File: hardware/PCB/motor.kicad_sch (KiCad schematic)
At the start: 56 parts, among them J3 Cutting Tool, U4 BSC050N04LSG

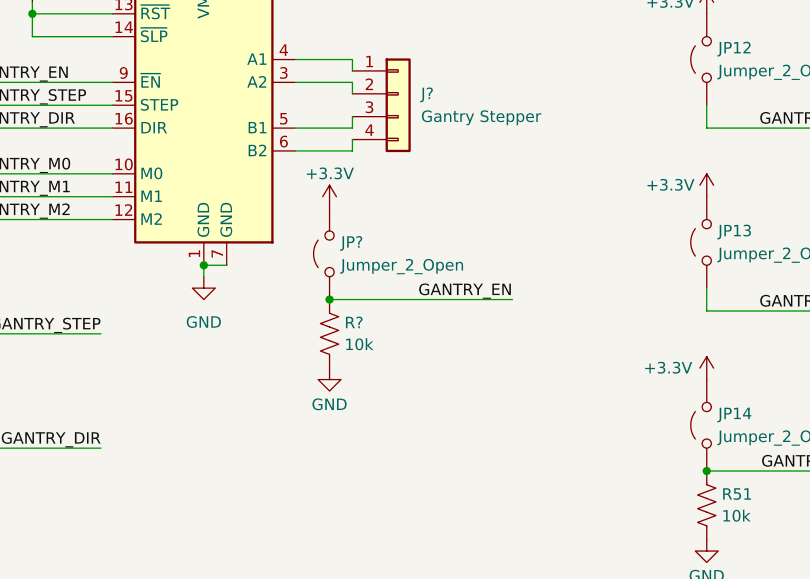
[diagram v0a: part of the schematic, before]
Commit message: Schematic - Motor Control Error
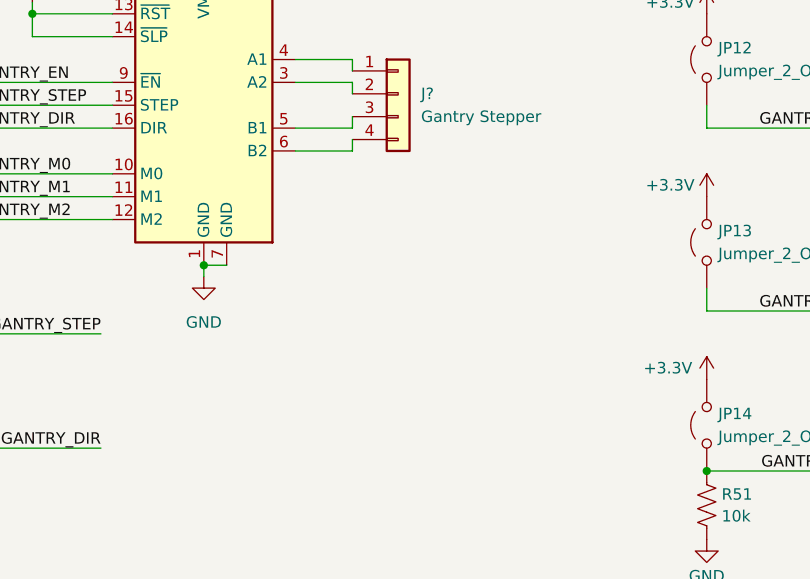
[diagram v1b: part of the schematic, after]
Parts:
- removed JP?: Jumper_2_Open, Connector_PinHeader_2.54mm:PinHeader_1x02_P2.54mm_Vertical, symbol Jumper:Jumper_2_Open
- removed R?: 10k, Resistor_SMD:R_0805_2012Metric, symbol Device:R_US
- added TP? (x2): TestPoint, symbol Connector:TestPoint
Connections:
- net EXTRUDER_DIR: now also TP?.1; no longer TP?.1
- net EXTRUDER_STEP: now also TP?.1; no longer TP?.1

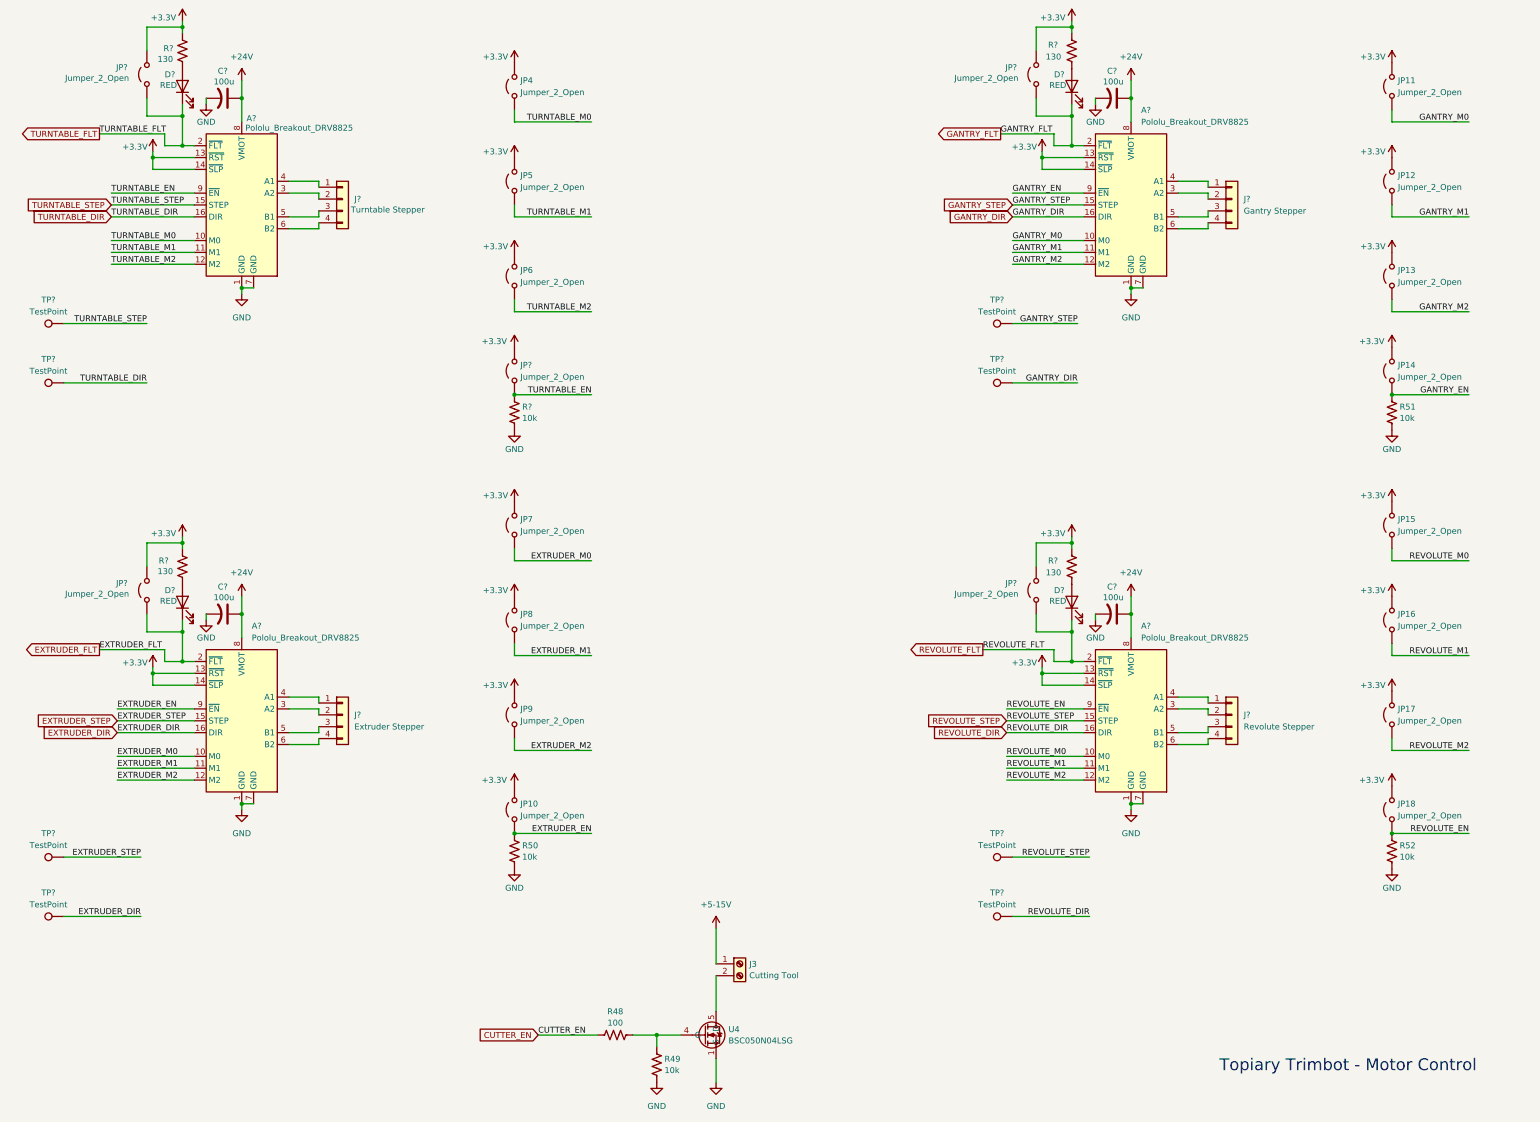
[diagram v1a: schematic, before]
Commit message: Synchronized schematic draft and reannotated all
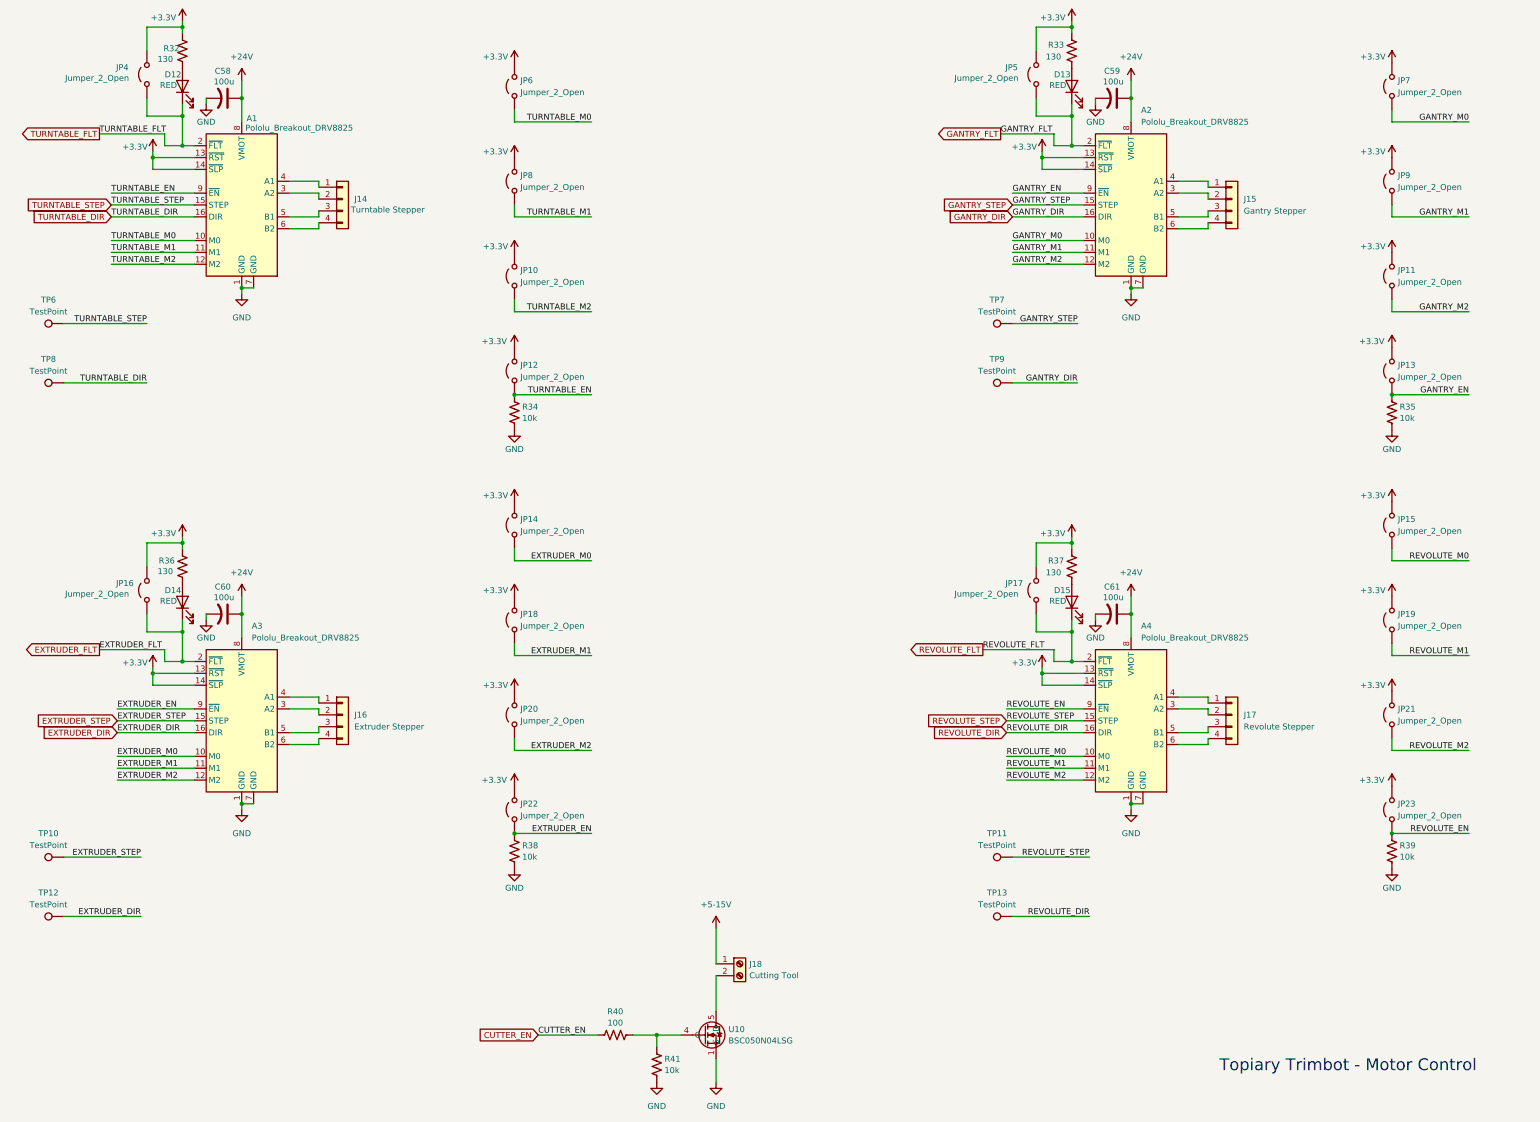
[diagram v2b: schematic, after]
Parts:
- J14, J15, J16, J17: renamed from J?; MANUFACTURER (none) -> Molex
- TP10, TP11, TP12, TP13, TP6, TP7, TP8, TP9: renamed from TP?; footprint (none) -> TestPoint:TestPoint_Pad_D1.5mm
- gave numbers to parts that had none: 22
- renumbered J3 to J18, JP6 to JP10, JP13 to JP11, JP14 to JP13, JP7 to JP14, JP8 to JP18, JP16 to JP19, JP9 to JP20, JP17 to JP21, JP10 to JP22, JP18 to JP23, JP4 to JP6, JP11 to JP7, JP5 to JP8, JP12 to JP9, R51 to R35, R50 to R38, R52 to R39, R48 to R40, R49 to R41, U4 to U10

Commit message: Finish first pass placement of parts on PCB, several updates and fixes to schematic included
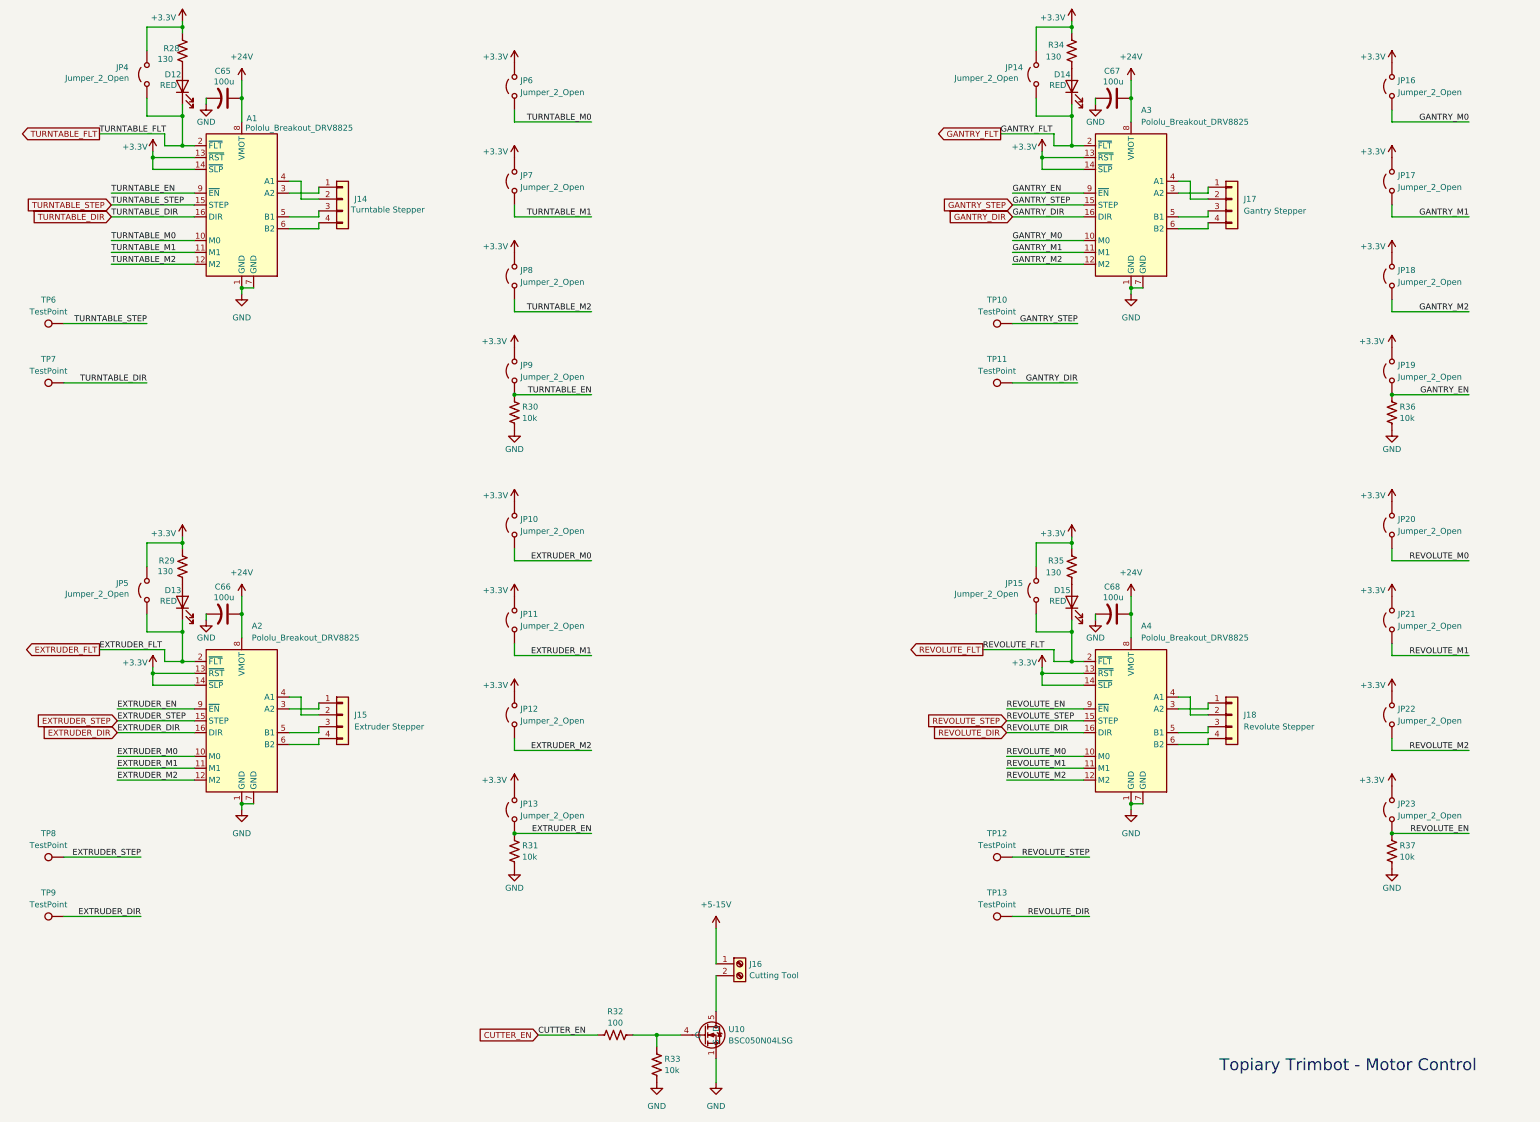
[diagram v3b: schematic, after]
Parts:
- renumbered A3 to A2, A2 to A3, C58 to C65, C60 to C66, C59 to C67, C61 to C68, D14 to D13, D13 to D14, J16 to J15, J18 to J16, J15 to J17, J17 to J18, JP14 to JP10, JP18 to JP11, JP20 to JP12, JP22 to JP13, JP5 to JP14, JP17 to JP15, JP7 to JP16, JP9 to JP17, JP11 to JP18, JP13 to JP19, JP15 to JP20, JP19 to JP21, JP21 to JP22, JP16 to JP5, JP8 to JP7, JP10 to JP8, JP12 to JP9, R32 to R28, R36 to R29, R34 to R30, R38 to R31, R40 to R32, R41 to R33, R33 to R34, R37 to R35, R35 to R36, R39 to R37, TP7 to TP10, TP9 to TP11, TP11 to TP12, TP8 to TP7, TP10 to TP8, TP12 to TP9
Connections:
- net at A4.3 (A2): now also J18.1 (Pin_1); no longer J18.2 (Pin_2)
- net at A4.4 (A1): now also J18.2 (Pin_2); no longer J18.1 (Pin_1)
- net at A2.3 (A2): now also J15.1 (Pin_1); no longer J15.2 (Pin_2)
- net at A2.4 (A1): now also J15.2 (Pin_2); no longer J15.1 (Pin_1)
- net at A3.3 (A2): now also J17.1 (Pin_1); no longer J17.2 (Pin_2)
- net at A3.4 (A1): now also J17.2 (Pin_2); no longer J17.1 (Pin_1)
- net at A1.3 (A2): now also J14.1 (Pin_1); no longer J14.2 (Pin_2)
- net at A1.4 (A1): now also J14.2 (Pin_2); no longer J14.1 (Pin_1)

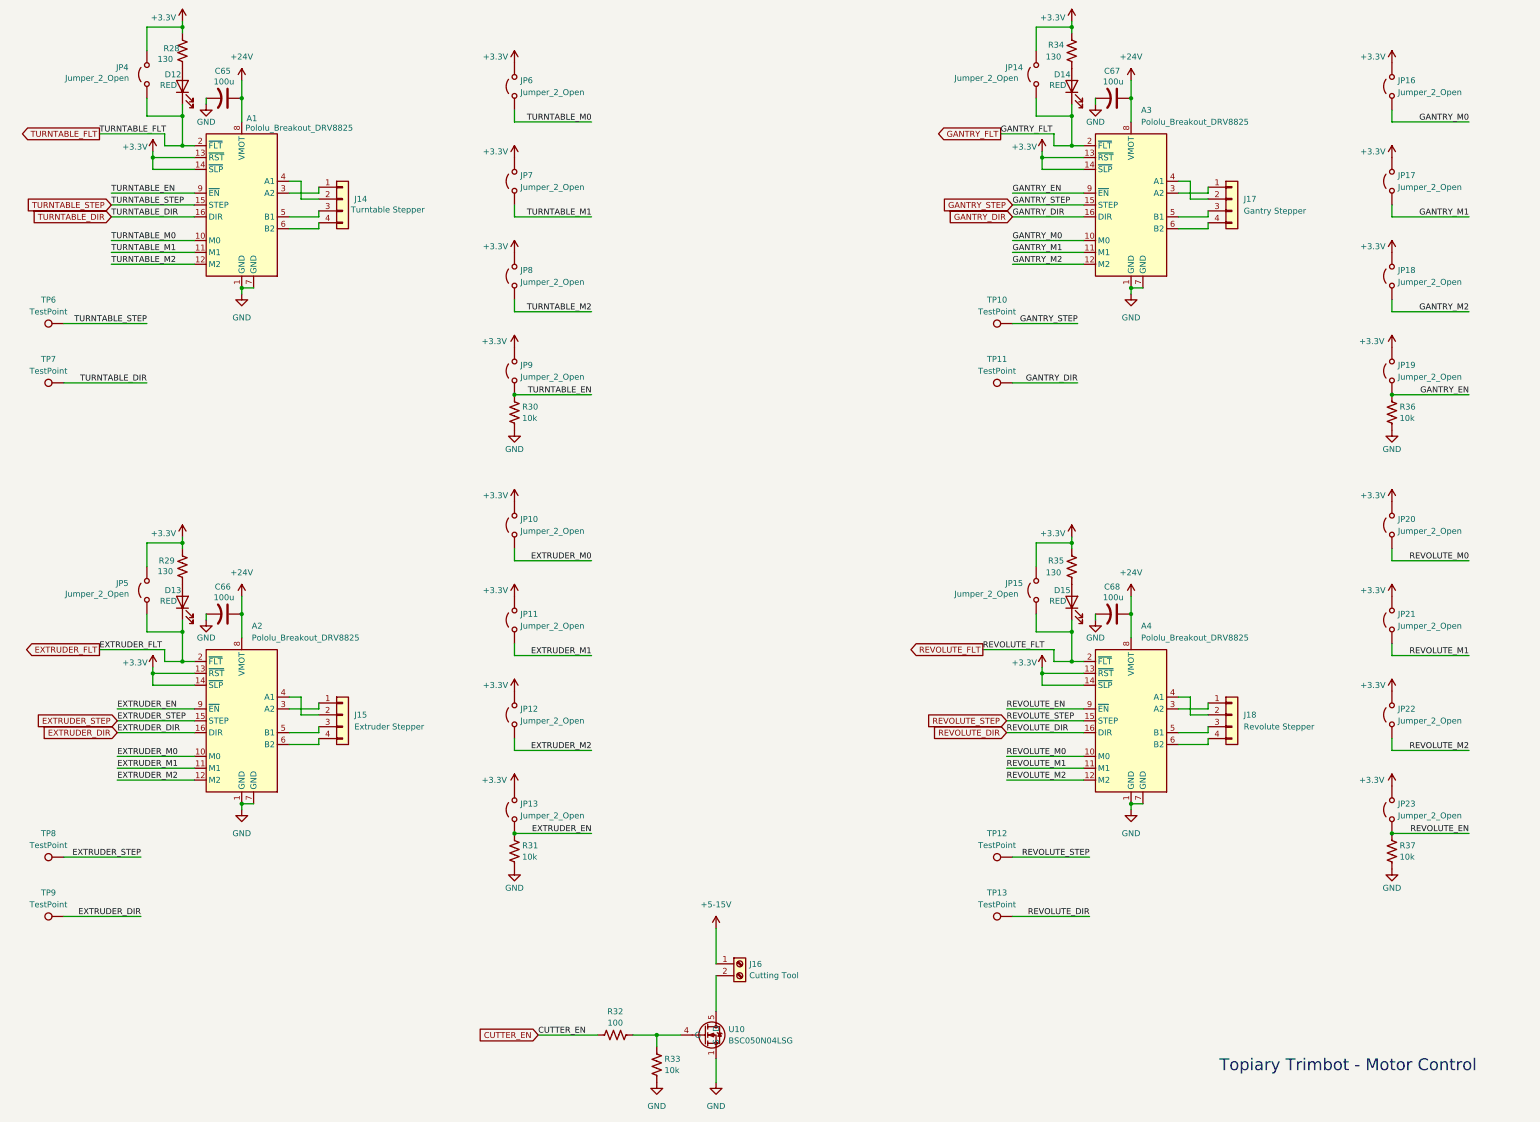
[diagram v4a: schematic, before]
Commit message: Continue layout, including swapping to linear BL driver
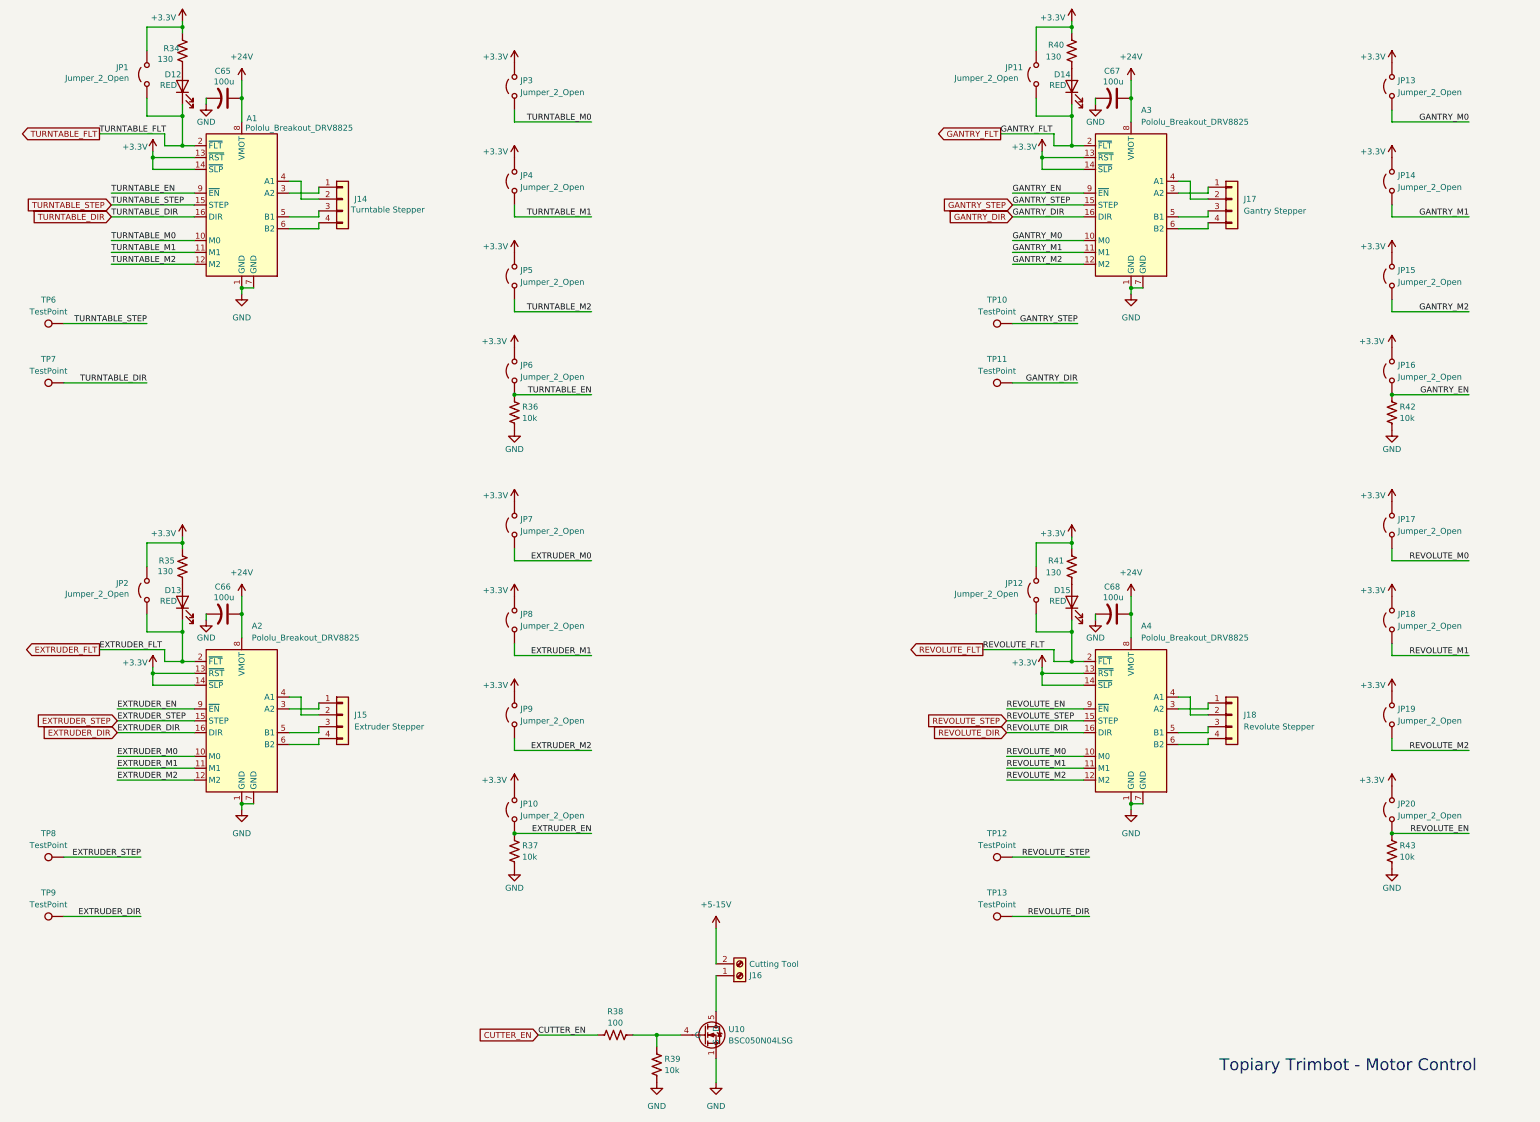
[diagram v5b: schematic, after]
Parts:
- renumbered JP4 to JP1, JP13 to JP10, JP14 to JP11, JP15 to JP12, JP16 to JP13, JP17 to JP14, JP18 to JP15, JP19 to JP16, JP20 to JP17, JP21 to JP18, JP22 to JP19, JP5 to JP2, JP23 to JP20, JP6 to JP3, JP7 to JP4, JP8 to JP5, JP9 to JP6, JP10 to JP7, JP11 to JP8, JP12 to JP9, R28 to R34, R29 to R35, R30 to R36, R31 to R37, R32 to R38, R33 to R39, R34 to R40, R35 to R41, R36 to R42, R37 to R43
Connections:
- net +5-15V: now also J16.2 (Pin_2); no longer J16.1 (Pin_1)
- net at U10.5 (D): now also J16.1 (Pin_1); no longer J16.2 (Pin_2)

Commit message: all part numbers
may need revisions
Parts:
- C65, C66, C67, C68: MANUFACTURER (none) -> Nichicon
- D12, D13, D14, D15: MANUFACTURER (none) -> Wurth; Manufacturer_Part_Number (none) -> 150080RS75000
- J16: MANUFACTURER (none) -> TE Connectivity AMP Connectors
- JP1, JP10, JP11, JP12, JP13, JP14, JP15, JP16, JP17, JP18, JP19, JP2, JP20, JP3, JP4, JP5, JP6, JP7, JP8, JP9: MANUFACTURER (none) -> Wurth; Manufacturer_Part_Number (none) -> 61300211121
- R34, R35, R40, R41: MANUFACTURER (none) -> Yageo; Manufacturer_Part_Number (none) -> RC0805JR-07130RL
- R36, R37, R39, R42, R43: MANUFACTURER (none) -> Yageo; Manufacturer_Part_Number (none) -> RC0805JR-0710KL
- R38: MANUFACTURER (none) -> Yageo; Manufacturer_Part_Number (none) -> RC0805JR-07100RL
- TP10, TP11, TP12, TP13, TP6, TP7, TP8, TP9: now left out of the parts list
- U10: MANUFACTURER (none) -> Infineon
